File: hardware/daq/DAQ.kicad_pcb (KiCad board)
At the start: 4 copper layers, 112 x 125 mm, 190 parts, among them J1 ICD15S13E4GX00LF, J2 ICD15S13E4GX00LF, J4 ICD15S13E4GX00LF, J5 ICD15S13E4GX00LF, P1 0022272021, U1 ADS124S08IRHBT, U11 SN74AHCT125RGYR, U2 ADS124S08IRHBT, U3 LT6654BMPS6-5-TRMPBF, U4 LM1086IS-5.0_NOPB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

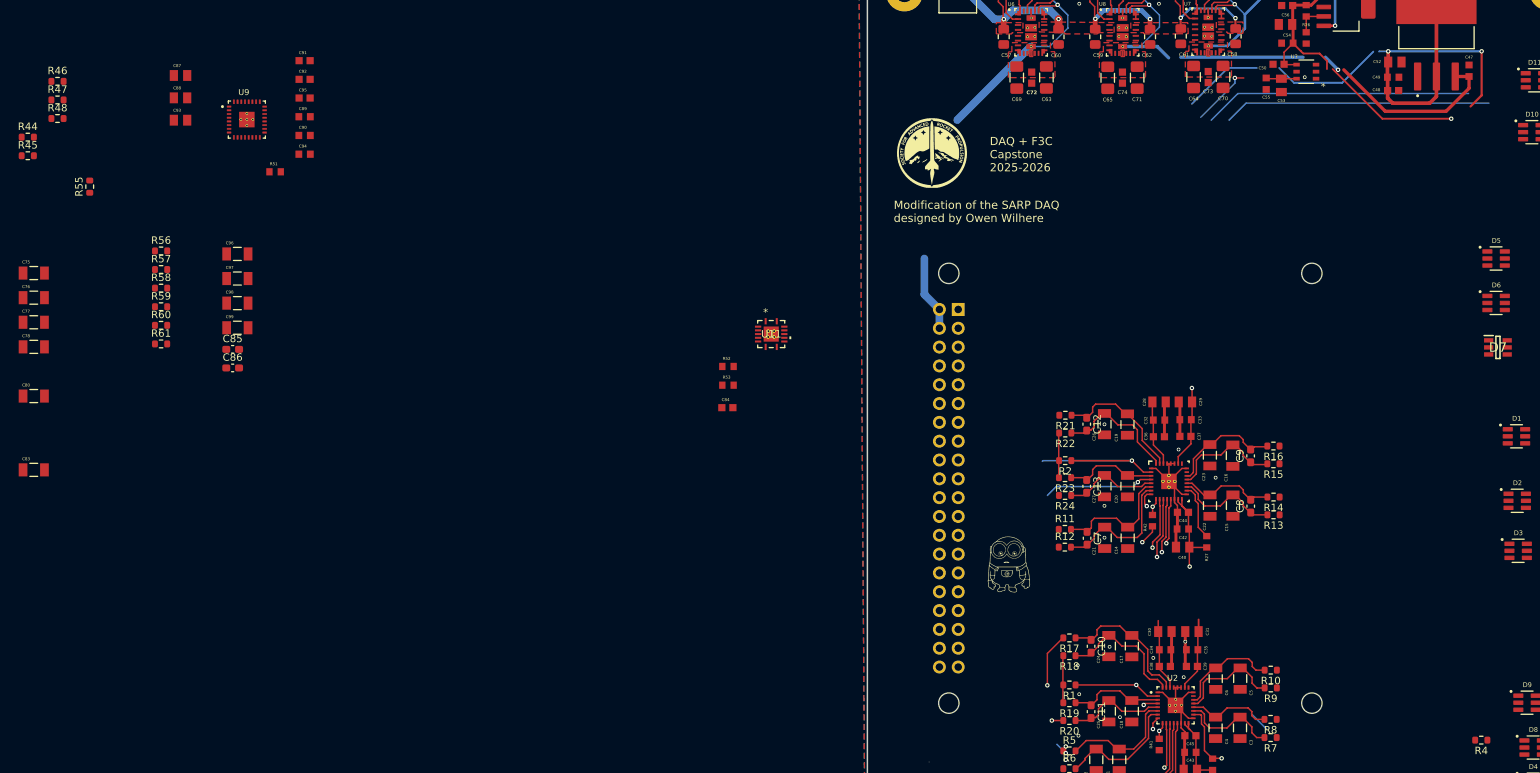
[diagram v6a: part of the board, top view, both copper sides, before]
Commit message: almost finished arranging ADC3 components
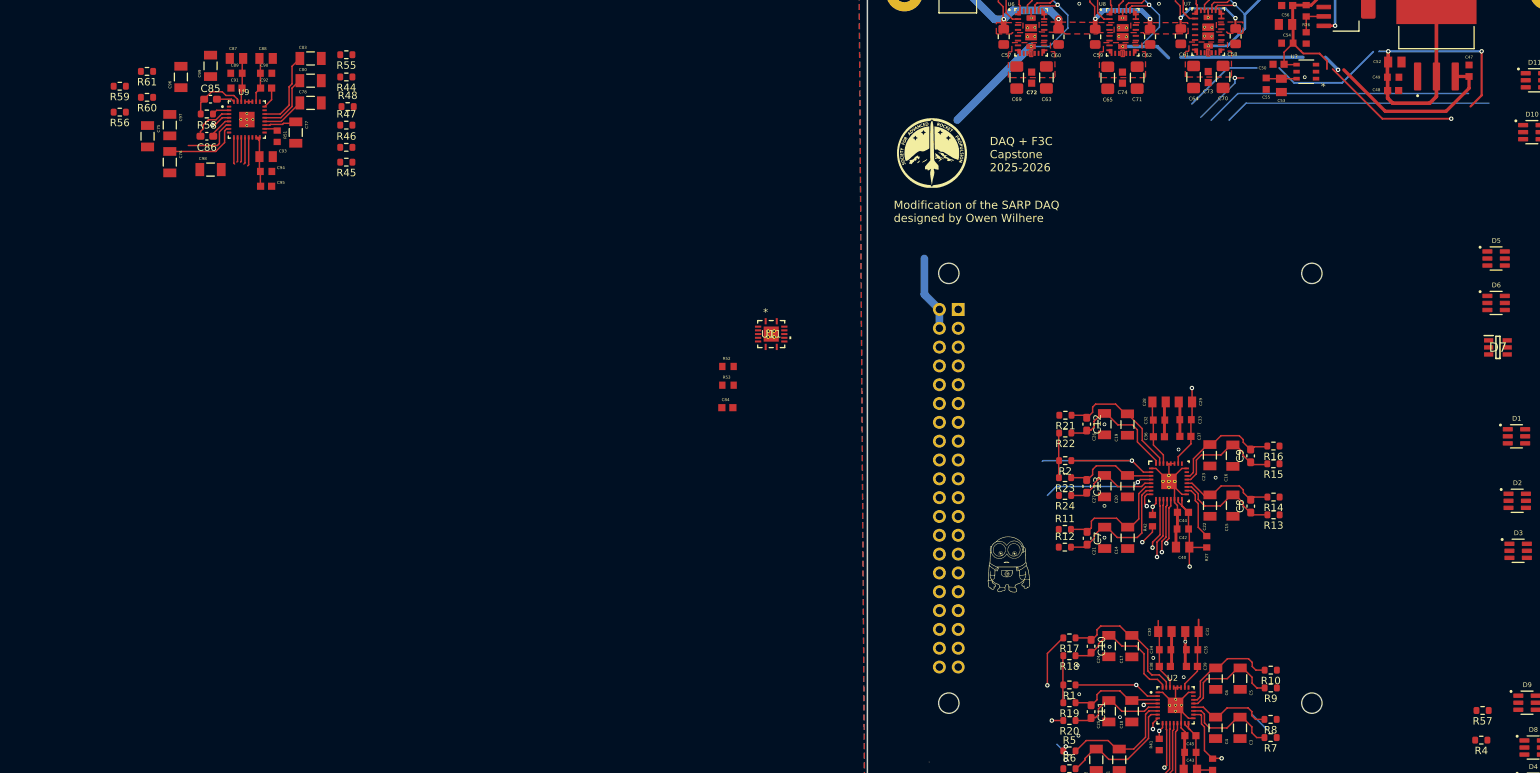
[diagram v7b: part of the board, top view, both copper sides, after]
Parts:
- moved R57 188.0 mm to (149.3, 135.5), turned to 180 degrees
- moved C83 66.9 mm to (-8.83, 47.5)
- moved C80 56.6 mm to (-8.83, 50.5)
- moved C78 49.8 mm to (-8.83, 53.5)
- moved R44 43.7 mm to (-4.00, 50.0), turned to 180 degrees
- moved C77 43.7 mm to (-10.8, 57.5), turned to -90 degrees
- moved R45 43.0 mm to (-4.00, 61.5), turned to 180 degrees
- moved R46 40.0 mm to (-4.00, 59.5), turned to 180 degrees
- moved R48 39.2 mm to (-3.83, 54.0), turned to 180 degrees
- moved R47 39.1 mm to (-4.00, 56.5), turned to 180 degrees
- moved R55 38.9 mm to (-4.00, 47.0), turned to 180 degrees
- moved R61 36.8 mm to (-30.9, 49.2), turned to 180 degrees
- moved C99 35.5 mm to (-22.3, 48.5), turned to 90 degrees
- moved C85 33.9 mm to (-22.3, 53.0)
- moved C86 31.5 mm to (-22.8, 58.0)
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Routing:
- net Net-(U9-GPIO0_AIN8): track 0.00 -> 10.7 mm
- net Net-(U9-AIN0): track 0.00 -> 10.2 mm
- net Net-(U9-GPIO1_AIN9): track 0.00 -> 8.28 mm
- net +3.3V: track 27.0 -> 34.9 mm
- net Net-(U9-REFN1_AIN7): track 0.00 -> 7.87 mm
- net Net-(U9-AIN1): track 0.00 -> 7.57 mm
- net +5Vs: track 96.1 -> 102.3 mm
- net 5V REF: track 34.0 -> 39.9 mm
- net Net-(U9-GPIO2_AIN10): track 0.00 -> 5.79 mm
- net Net-(U9-AIN4): track 0.00 -> 5.77 mm
- net Net-(U9-GPIO3_AIN11): track 0.00 -> 4.38 mm
- net /DRDY_N3: track 0.00 -> 3.91 mm
- net GND: track 64.5 -> 68.4 mm
- net /MISO: track 15.0 -> 18.7 mm
- net /CE3: track 0.00 -> 3.64 mm
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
